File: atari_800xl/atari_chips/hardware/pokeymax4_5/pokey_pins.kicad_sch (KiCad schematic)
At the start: 4 parts, among them J2 Conn_01x14_Pin

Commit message: kicad 10 upgrade
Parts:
- IC1: value ~ -> (none)

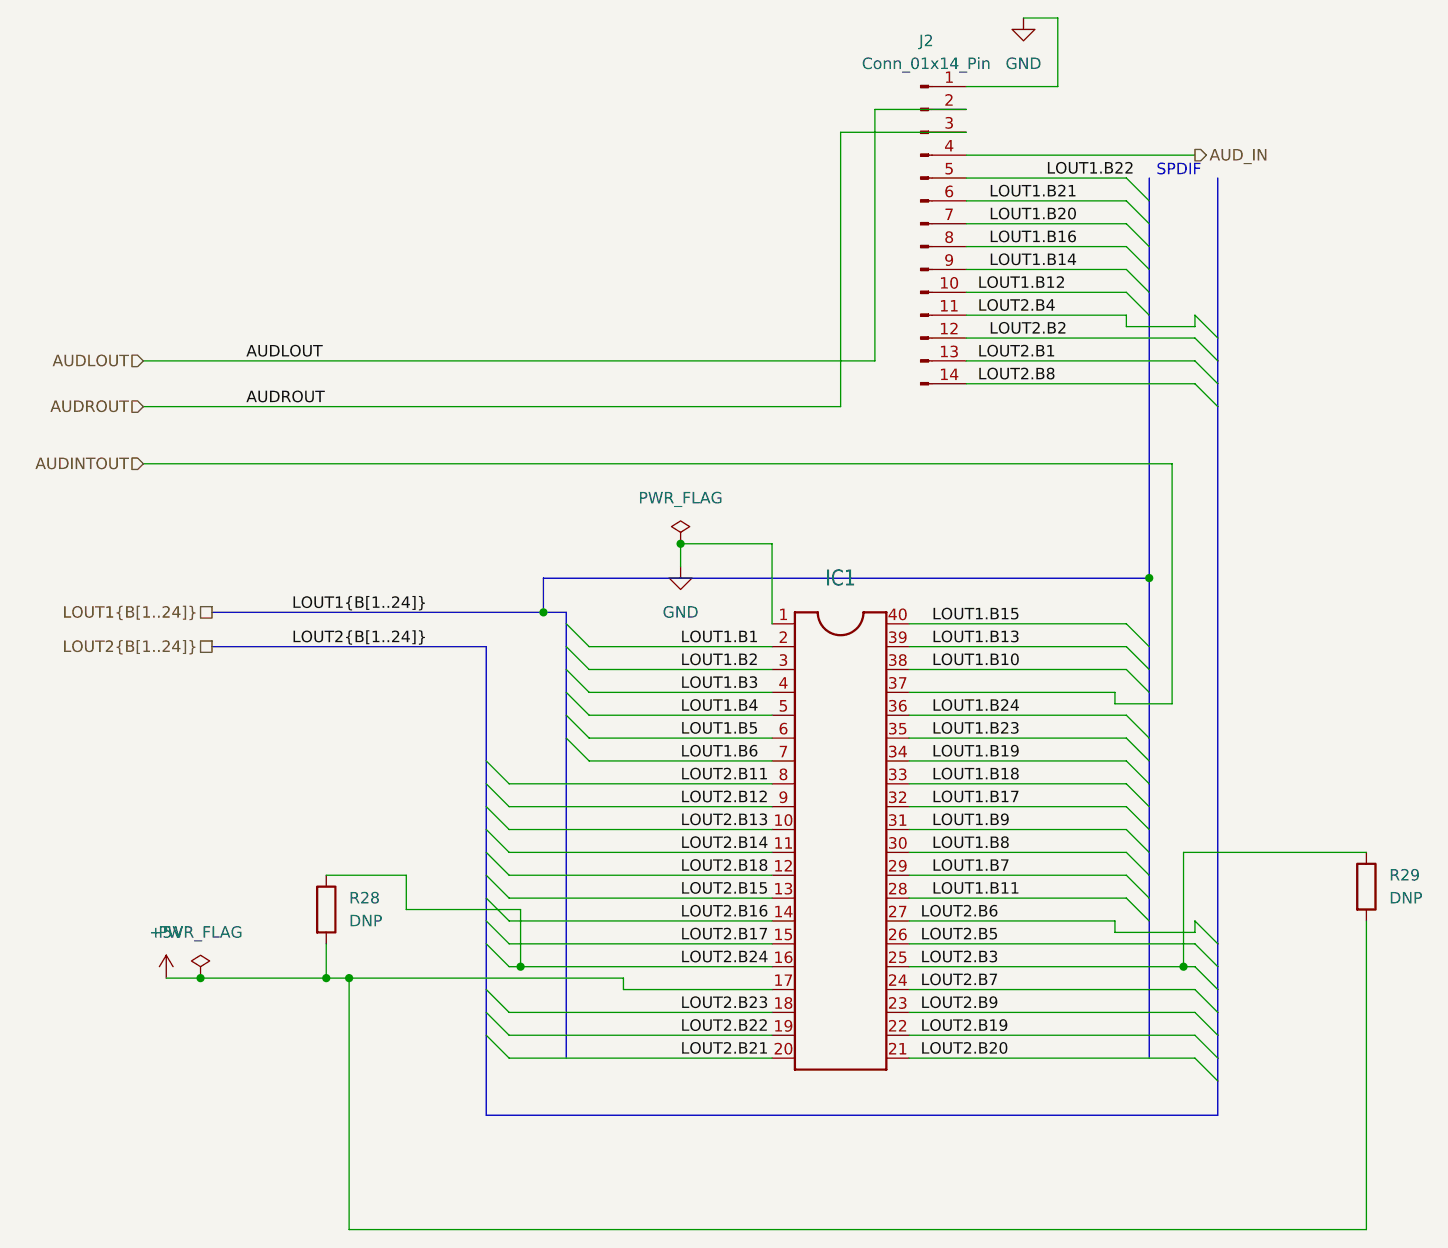
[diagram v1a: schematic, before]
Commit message: 4.55. Got AI to help me improve a few minor things. Regulator mode, extra decoupling for DAC, distances from edge, gnd/power plane switched, track spacing for a few important lines, bigger cap on 2.5v reg, shorter critical traces on 3.3v reg. Also it double checked the sallen key filter. Switched to the JLCPCB plugin for simpler part management.
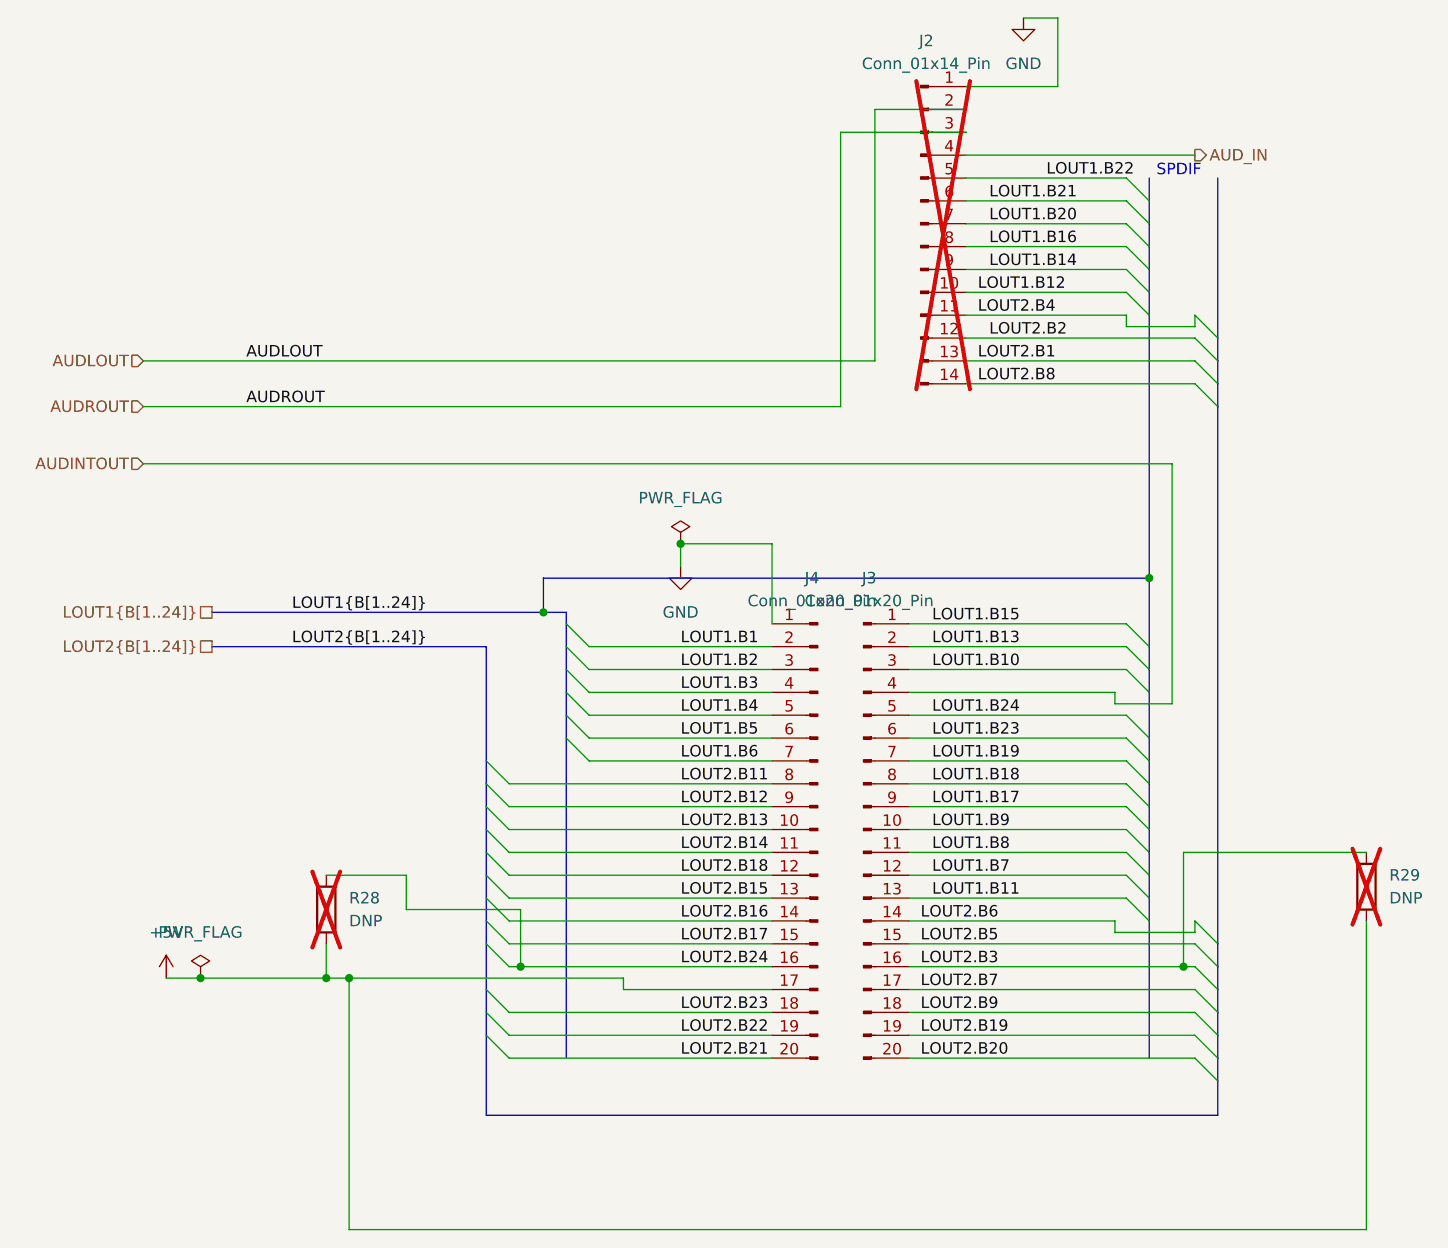
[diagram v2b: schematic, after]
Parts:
- removed IC1: (no value), ic-package:DIL40, symbol ic-package:DIL40
- added J3, J4: Conn_01x20_Pin, Connector_PinSocket_2.54mm:PinSocket_1x20_P2.54mm_Vertical, symbol Connector:Conn_01x20_Pin
- J2, R28, R29: now not fitted; now left out of the parts list
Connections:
- net +5V: now also J4.17 (Pin_17)
- net AUDINTOUT: now also J3.4 (Pin_4)
- net GND: now also J4.1 (Pin_1)
- net LOUT1.B1: now also J4.2 (Pin_2)
- net LOUT1.B10: now also J3.3 (Pin_3)
- net LOUT1.B11: now also J3.13 (Pin_13)
- net LOUT1.B13: now also J3.2 (Pin_2)
- net LOUT1.B15: now also J3.1 (Pin_1)
- net LOUT1.B17: now also J3.9 (Pin_9)
- net LOUT1.B18: now also J3.8 (Pin_8)
- net LOUT1.B19: now also J3.7 (Pin_7)
- net LOUT1.B2: now also J4.3 (Pin_3)
- net LOUT1.B23: now also J3.6 (Pin_6)
- net LOUT1.B24: now also J3.5 (Pin_5)
- net LOUT1.B3: now also J4.4 (Pin_4)
- net LOUT1.B4: now also J4.5 (Pin_5)
- net LOUT1.B5: now also J4.6 (Pin_6)
- net LOUT1.B6: now also J4.7 (Pin_7)
- net LOUT1.B7: now also J3.12 (Pin_12)
- net LOUT1.B8: now also J3.11 (Pin_11)
- net LOUT1.B9: now also J3.10 (Pin_10)
- net LOUT2.B11: now also J4.8 (Pin_8)
- net LOUT2.B12: now also J4.9 (Pin_9)
- net LOUT2.B13: now also J4.10 (Pin_10)
- net LOUT2.B14: now also J4.11 (Pin_11)
- net LOUT2.B15: now also J4.13 (Pin_13)
- net LOUT2.B16: now also J4.14 (Pin_14)
- net LOUT2.B17: now also J4.15 (Pin_15)
- net LOUT2.B18: now also J4.12 (Pin_12)
- net LOUT2.B19: now also J3.19 (Pin_19)
- net LOUT2.B20: now also J3.20 (Pin_20)
- net LOUT2.B21: now also J4.20 (Pin_20)
- net LOUT2.B22: now also J4.19 (Pin_19)
- net LOUT2.B23: now also J4.18 (Pin_18)
- net LOUT2.B24: now also J4.16 (Pin_16)
- net LOUT2.B3: now also J3.16 (Pin_16)
- net LOUT2.B5: now also J3.15 (Pin_15)
- net LOUT2.B6: now also J3.14 (Pin_14)
- net LOUT2.B7: now also J3.17 (Pin_17)
- net LOUT2.B9: now also J3.18 (Pin_18)
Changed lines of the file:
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@@
 		(body_style 1)
 		(exclude_from_sim no)
-		(in_bom yes)
+		(in_bom no)
 		(on_board yes)
 		(in_pos_files yes)
-		(dnp no)
+		(dnp yes)
 		(fields_autoplaced yes)
 		(property "Reference" "R28"
@@
 	)
 	(symbol
-		(lib_id "Connector:Conn_01x14_Pin")
-		(at 111.76 36.83 0)
+		(lib_id "Connector:Conn_01x20_Pin")
+		(at 100.33 104.14 0)
+		(mirror y)
 		(unit 1)
 		(body_style 1)
@@
 		(in_pos_files yes)
 		(dnp no)
+		(property "Reference" "J4"
+			(at 99.695 76.2 0)
+			(show_name no)
+			(do_not_autoplace no)
+			(effects
+				(font
+					(size 1.27 1.27)
+				)
+			)
+		)
+		(property "Value" "Conn_01x20_Pin"
+			(at 99.695 78.74 0)
+			(show_name no)
+			(do_not_autoplace no)
+			(effects
+				(font
+					(size 1.27 1.27)
+				)
+			)
+		)
+		(property "Footprint" "Connector_PinSocket_2.54mm:PinSocket_1x20_P2.54mm_Vertical"
+			(at 100.33 104.14 0)
+			(hide yes)
+			(show_name no)
+			(do_not_autoplace no)
+			(effects
+				(font
+					(size 1.27 1.27)
+				)
+			)
+		)
+		(property "Datasheet" ""
+			(at 100.33 104.14 0)
+			(hide yes)
+			(show_name no)
+			(do_not_autoplace no)
+			(effects
+				(font
+					(size 1.27 1.27)
+				)
+			)
+		)
+		(property "Description" "Generic connector, single row, 01x20, script generated"
+			(at 100.33 104.14 0)
+			(hide yes)
+			(show_name no)
+			(do_not_autoplace no)
+			(effects
+				(font
+					(size 1.27 1.27)
+				)
+			)
+		)
+		(property "KiLib_Generator" "connector/pin_header_socket"
+			(at 100.33 104.14 0)
+			(hide yes)
+			(show_name no)
+			(do_not_autoplace no)
+			(effects
+				(font
+					(size 1.27 1.27)
+				)
+			)
+		)
+		(property "LCSC" "C5156447"
+			(at 100.33 104.14 0)
+			(hide yes)
+			(show_name no)
+			(do_not_autoplace no)
+			(effects
+				(font
+					(size 1.27 1.27)
+				)
+			)
+		)
+		(pin "1"
+		)
+		(pin "6"
+		)
+		(pin "5"
+		)
+		(pin "13"
+		)
+		(pin "7"
+		)
+		(pin "9"
+		)
+		(pin "12"
+		)
+		(pin "11"
+		)
+		(pin "10"
+		)
+		(pin "2"
+		)
+		(pin "4"
+		)
+		(pin "14"
+		)
+		(pin "3"
+		)
+		(pin "8"
+		)
+		(pin "20"
+		)
+		(pin "17"
+		)
+		(pin "16"
+		)
+		(pin "19"
+		)
+		(pin "18"
+		)
+		(pin "15"
+		)
+		(instances
+			(project "pokeymax4_5"
+				(path "/f8f92944-710a-49a0-a698-f840e5f20e15/473fb442-f6a6-4f3e-b077-9a313beb11d5"
+					(reference "J4")
+					(unit 1)
+				)
+			)
+		)
+	)
+	(symbol
+		(lib_id "Connector:Conn_01x14_Pin")
+		(at 111.76 36.83 0)
+		(unit 1)
+		(body_style 1)
+		(exclude_from_sim no)
+		(in_bom no)
+		(on_board yes)
+		(in_pos_files yes)
+		(dnp yes)
 		(fields_autoplaced yes)
 		(property "Reference" "J2"
@@
 	)
 	(symbol
-		(lib_id "ic-package:DIL40")
-		(at 102.87 104.14 0)
-		(unit 1)
-		(body_style 1)
-		(exclude_from_sim no)
-		(in_bom yes)
-		(on_board yes)
-		(in_pos_files yes)
-		(dnp no)
-		(fields_autoplaced yes)
-		(property "Reference" "IC1"
-			(at 102.87 76.2 0)
-			(show_name no)
-			(do_not_autoplace no)
-			(effects
-				(font
-					(size 1.778 1.5113)
-				)
-			)
-		)
-		(property "Value" ""
-			(at 102.87 78.74 0)
-			(show_name no)
-			(do_not_autoplace no)
-			(effects
-				(font
-					(size 1.778 1.5113)
-				)
-			)
-		)
-		(property "Footprint" "ic-package:DIL40"
-			(at 102.87 104.14 0)
-			(hide yes)
-			(show_name no)
-			(do_not_autoplace no)
-			(effects
-				(font
-					(size 1.27 1.27)
-				)
-			)
-		)
-		(property "Datasheet" ""
-			(at 102.87 104.14 0)
-			(hide yes)
-			(show_name no)
-			(do_not_autoplace no)
-			(effects
-				(font
-					(size 1.27 1.27)
-				)
-			)
-		)
-		(property "Description" "Dual In Line"
-			(at 102.87 104.14 0)
-			(hide yes)
-			(show_name no)
-			(do_not_autoplace no)
-			(effects
-				(font
-					(size 1.27 1.27)
-				)
-			)
-		)
-		(pin "28"
-		)
-		(pin "11"
-		)
-		(pin "13"
-		)
-		(pin "12"
-		)
-		(pin "25"
-		)
-		(pin "40"
-		)
-		(pin "33"
-		)
-		(pin "2"
-		)
-		(pin "27"
-		)
-		(pin "30"
-		)
-		(pin "19"
-		)
-		(pin "29"
-		)
-		(pin "15"
-		)
-		(pin "3"
-		)
-		(pin "17"
-		)
-		(pin "34"
-		)
-		(pin "31"
-		)
-		(pin "35"
-		)
-		(pin "20"
-		)
-		(pin "37"
-		)
-		(pin "22"
-		)
-		(pin "24"
-		)
-		(pin "18"
-		)
-		(pin "10"
-		)
-		(pin "32"
-		)
-		(pin "23"
-		)
-		(pin "5"
-		)
-		(pin "7"
-		)
-		(pin "21"
-		)
-		(pin "8"
-		)
-		(pin "26"
-		)
-		(pin "16"
-		)
-		(pin "1"
-		)
-		(pin "36"
-		)
-		(pin "4"
-		)
-		(pin "6"
-		)
-		(pin "38"
-		)
-		(pin "14"
-		)
-		(pin "39"
-		)
-		(pin "9"
-		)
-		(instances
-			(project "pokeymax4_5"
-				(path "/f8f92944-710a-49a0-a698-f840e5f20e15/473fb442-f6a6-4f3e-b077-9a313beb11d5"
-					(reference "IC1")
-					(unit 1)
-				)
-			)
-		)
-	)
-	(symbol
 		(lib_id "power:+5V")
 		(at 27.94 120.65 0)
@@
 		(body_style 1)
 		(exclude_from_sim no)
-		(in_bom yes)
+		(in_bom no)
 		(on_board yes)
 		(in_pos_files yes)
-		(dnp no)
+		(dnp yes)
 		(fields_autoplaced yes)
 		(property "Reference" "R29"
@@
 					(unit 1)
 				)
+			)
+		)
+	)
+	(symbol
+		(lib_id "Connector:Conn_01x20_Pin")
+		(at 105.41 104.14 0)
+		(unit 1)
+		(body_style 1)
+		(exclude_from_sim no)
+		(in_bom yes)
+		(on_board yes)
+		(in_pos_files yes)
+		(dnp no)
+		(fields_autoplaced yes)
+		(property "Reference" "J3"
+			(at 106.045 76.2 0)
+			(show_name no)
+			(do_not_autoplace no)
+			(effects
+				(font
+					(size 1.27 1.27)
+				)
+			)
+		)
+		(property "Value" "Conn_01x20_Pin"
+			(at 106.045 78.74 0)
+			(show_name no)
+			(do_not_autoplace no)
+			(effects
+				(font
+					(size 1.27 1.27)
+				)
+			)
+		)
+		(property "Footprint" "Connector_PinSocket_2.54mm:PinSocket_1x20_P2.54mm_Vertical"
+			(at 105.41 104.14 0)
+			(hide yes)
+			(show_name no)
+			(do_not_autoplace no)
+			(effects
+				(font
+					(size 1.27 1.27)
+				)
+			)
+		)
+		(property "Datasheet" ""
+			(at 105.41 104.14 0)
+			(hide yes)
+			(show_name no)
+			(do_not_autoplace no)
+			(effects
+				(font
+					(size 1.27 1.27)
+				)
+			)
+		)
+		(property "Description" "Generic connector, single row, 01x20, script generated"
+			(at 105.41 104.14 0)
+			(hide yes)
+			(show_name no)
+			(do_not_autoplace no)
+			(effects
+				(font
+					(size 1.27 1.27)
+				)
+			)
+		)
+		(property "KiLib_Generator" "connector/pin_header_socket"
+			(at 105.41 104.14 0)
+			(hide yes)
+			(show_name no)
+			(do_not_autoplace no)
+			(effects
+				(font
+					(size 1.27 1.27)
+				)
+			)
+		)
+		(property "LCSC" "C5156447"
+			(at 105.41 104.14 0)
+			(hide yes)
+			(show_name no)
+			(do_not_autoplace no)
+			(effects
+				(font
+					(size 1.27 1.27)
+				)
+			)
+		)
+		(pin "1"
+		)
+		(pin "6"
+		)
+		(pin "5"
+		)
+		(pin "13"
+		)
+		(pin "7"
+		)
+		(pin "9"
+		)
+		(pin "12"
+		)
+		(pin "11"
+		)
+		(pin "10"
+		)
+		(pin "2"
+		)
+		(pin "4"
+		)
+		(pin "14"
+		)
+		(pin "3"
+		)
+		(pin "8"
+		)
+		(pin "20"
+		)
+		(pin "17"
+		)
+		(pin "16"
+		)
+		(pin "19"
+		)
+		(pin "18"
+		)
+		(pin "15"
+		)
+		(instances
+			(project "pokeymax4_5"
+				(path "/f8f92944-710a-49a0-a698-f840e5f20e15/473fb442-f6a6-4f3e-b077-9a313beb11d5"
+					(reference "J3")
+					(unit 1)
+				)
